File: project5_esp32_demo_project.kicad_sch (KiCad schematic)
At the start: 0 parts

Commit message: 1.1.2 Lipo battery charger
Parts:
- added J1: SS-52400-002, SS-52400-002:BELFUSE_SS-52400-002, symbol SS-52400-002:SS-52400-002
- added J2: B2B-PH-SM4-TB, B2B-PH-SM4-TB:JST_B2B-PH-SM4-TB, symbol B2B-PH-SM4-TB:B2B-PH-SM4-TB
- added LED1: LTST-C170KRKT, LTST-C170KRKT:DIOC200X125X110, symbol LTST-C170KRKT:LTST-C170KRKT
- added LED2: LTST-C170GKT, LED_LTST-C170GKT_LTO, symbol LTST-C170GKT:LTST-C170GKT
- added LED3: LTST-C170TBKT, LTST-C170TBKT:DIOC200X125X110, symbol LTST-C170TBKT:LTST-C170TBKT
- added R1, R2: 10K, symbol Device:R
- added R3, R4: 5K1, symbol Device:R
- added R5: 2K, symbol Device:R
- added R6: 20K, symbol Device:R
- added R7, R8, R9: 470, symbol Device:R
- added U1: MCP73871-2CAI_ML, MCP73871-2CAI_ML:QFN50P400X400X100-21N, symbol MCP73871-2CAI_ML:MCP73871-2CAI_ML
- added VR1: LM1117MPX-3.3, LM1117MPX-3.3:VREG_LM1117MPX-3.3, symbol LM1117MPX-3.3:LM1117MPX-3.3
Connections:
- new net: R6.2, U1.12 (PROG3)
- new net: J1.A5 (CC1), R4.1
- new net: J1.B5 (CC2), R3.1
- new net: LED2.1, R9.1
- new net: LED1.-, R7.1
- new net: R7.2, U1.7 (STAT2)
- new net: R1.1, U1.9 (~{TE})
- new net: R9.2, U1.6 (~{PG})
- new net: LED3.-, R8.1
- new net: U1.1 (OUT), U1.20 (OUT)
- new net: R5.1, U1.13 (PROG1)
- new net: U1.14 (VBAT), U1.15 (VBAT)
- new net: U1.18 (IN), U1.19 (IN)
- new net: R2.1, U1.5 (THERM)
- new net: R8.2, U1.8 (STAT1/~{LBO})
- new net GND: J1.A1 (GNDA1), J1.A12 (GNDA2), J1.B1 (GNDB1), J1.B12 (GNDB2), J1.G1 (GND/SHIELD), J1.G2 (GND/SHIELD), J1.G3 (GND/SHIELD), J1.G4 (GND/SHIELD), J1.S1 (GND/SHIELD), J1.S2 (GND/SHIELD), J1.S3 (GND/SHIELD), J1.S4 (GND/SHIELD), R1.2, R2.2, R3.2, R4.2, R5.2, R6.1
- new net VSS: U1.10 (VSS), U1.11 (VSS), U1.21 (VSS)

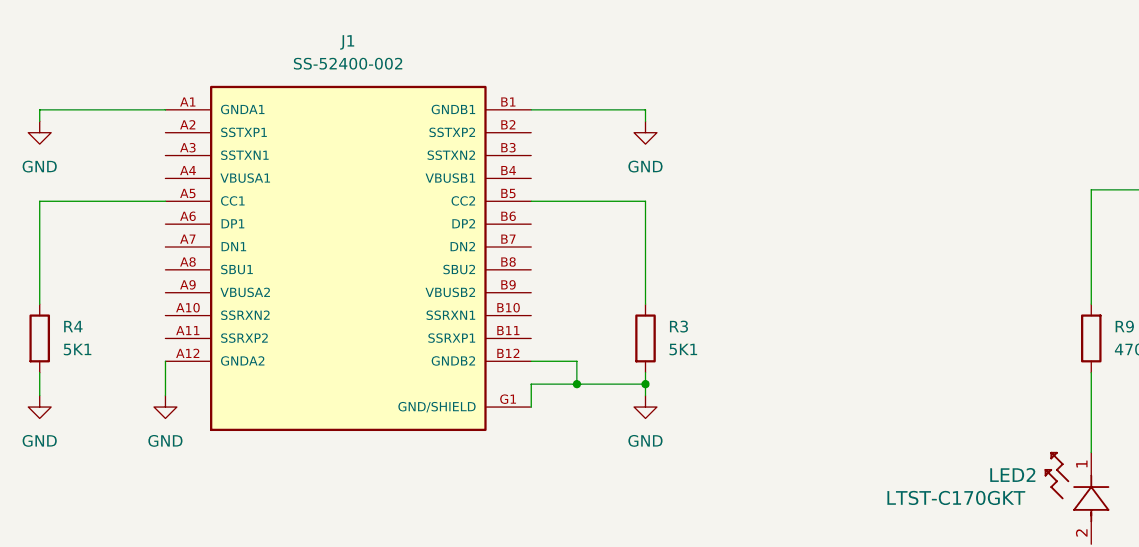
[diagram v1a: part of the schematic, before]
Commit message: 1.1.3 Design USB port subcircuit
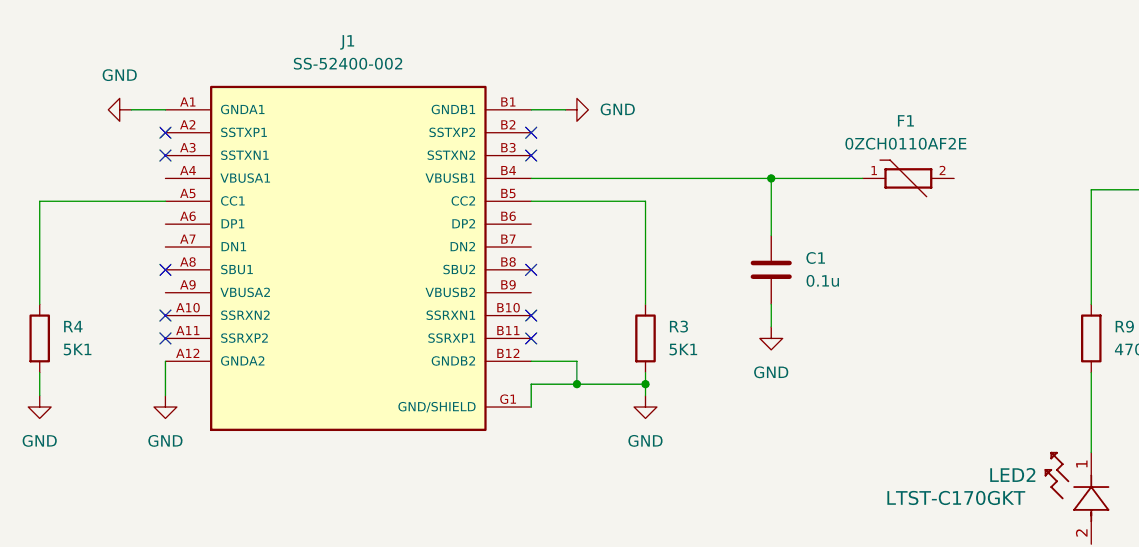
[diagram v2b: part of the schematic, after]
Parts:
- added C1: 0.1u, symbol Device:C
- added F1: 0ZCH0110AF2E, 0ZCH0110AF2E:FUSC3225X100N, symbol 0ZCH0110AF2E:0ZCH0110AF2E
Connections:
- net GND: now also C1.2
- net at J1.B4 (VBUSB1): now also C1.1, F1.1
- no-connect marks 0 -> 10

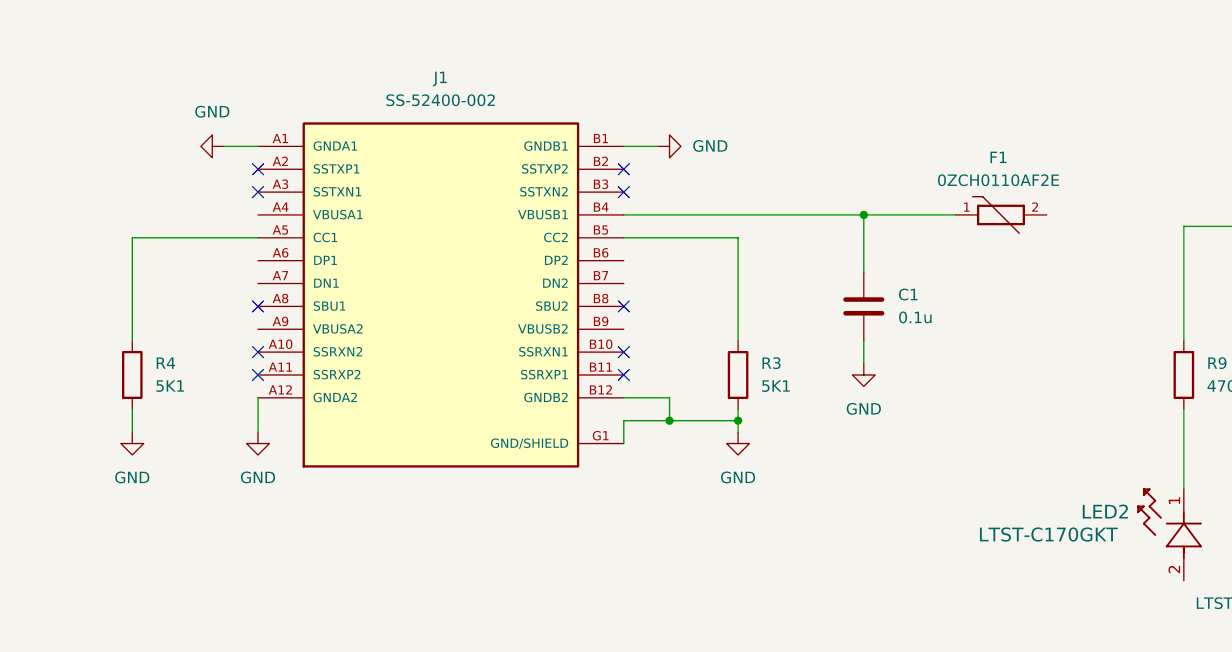
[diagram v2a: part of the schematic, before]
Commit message: 1.1.4 Create the first few nets
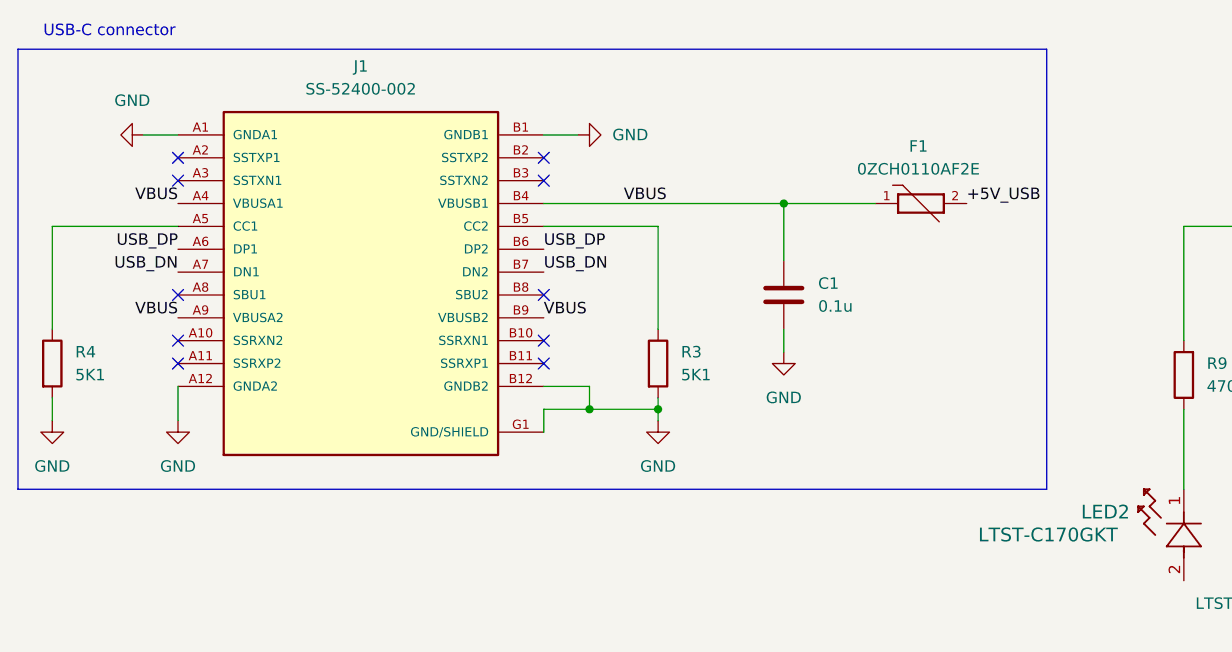
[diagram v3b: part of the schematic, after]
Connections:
- net VBUS: now reaches J1.A4 (VBUSA1)
- net VBUS: now also C1.1, F1.1, J1.A9 (VBUSA2), J1.B4 (VBUSB1), J1.B9 (VBUSB2)
- net USB_DP: now reaches J1.A6 (DP1)
- net USB_DP: now also J1.B6 (DP2)
- net USB_DN: now reaches J1.A7 (DN1)
- net USB_DN: now also J1.B7 (DN2)
- net +5V_USB: now reaches F1.2
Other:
- note added: "USB-C connector"
- moved on the sheet: C1, F1, J1, R3, R4

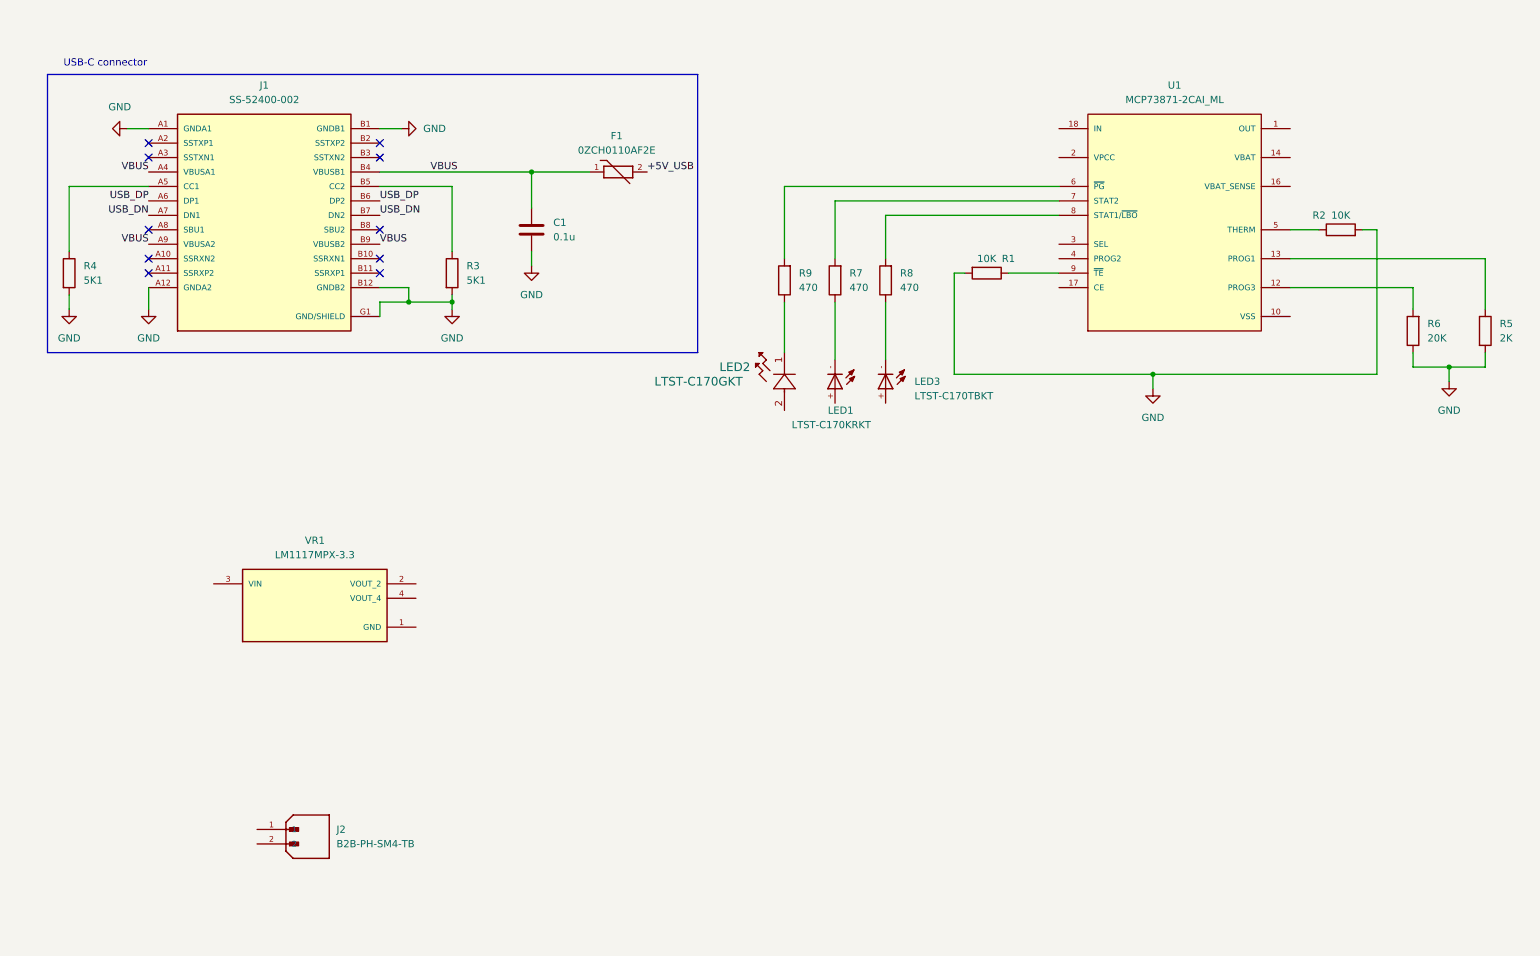
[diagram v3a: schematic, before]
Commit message: 1.1.5 Finish the design for the LiPo charger
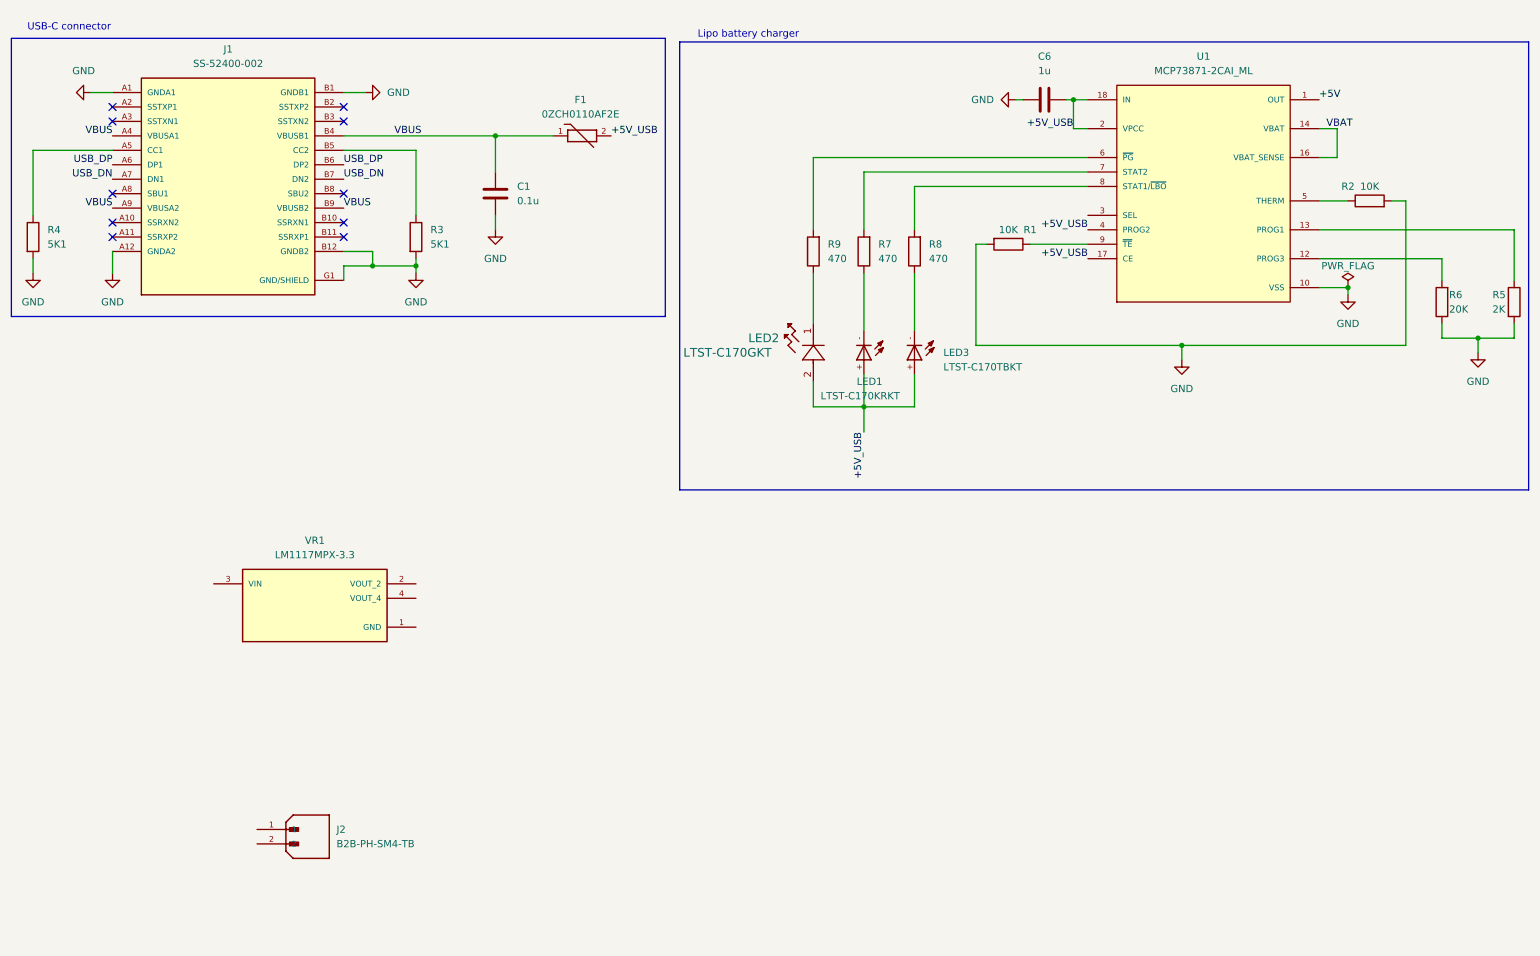
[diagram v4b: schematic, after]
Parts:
- added C6: 1u, symbol Device:C
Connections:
- net VSS is gone; now on net GND: U1.10 (VSS), U1.11 (VSS), U1.21 (VSS)
- net +5V_USB: now also LED1.+, LED2.2, LED3.+, U1.17 (CE), U1.18 (IN), U1.19 (IN), U1.2 (VPCC), U1.4 (PROG2), C6.2
- net GND: now also C6.1
- net +5V: now reaches U1.1 (OUT), U1.20 (OUT)
- net VBAT: now reaches U1.14 (VBAT), U1.15 (VBAT)
- net VBAT: now also U1.16 (VBAT_SENSE)
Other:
- note added: "Lipo battery charger"
- moved on the sheet: C1, F1, J1, LED1, LED2, LED3, R1, R2, R3, R4, R5, R6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

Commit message: 1.1.6 Design the voltage regulator subcircuit
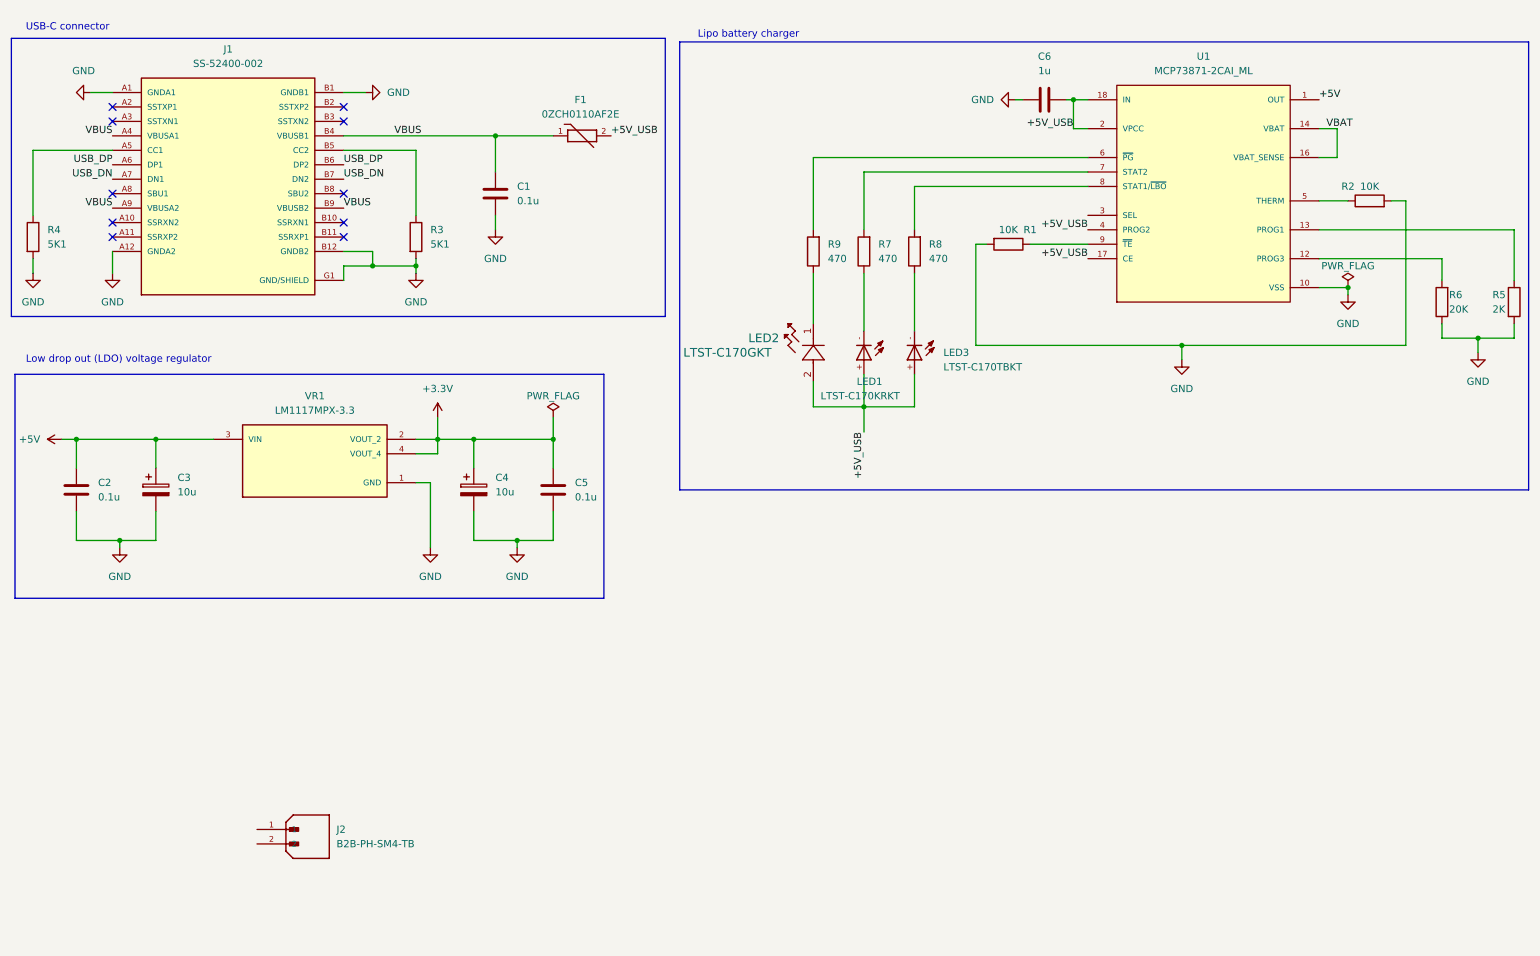
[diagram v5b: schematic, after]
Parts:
- added C2, C5: 0.1u, symbol Device:C
- added C3, C4: 10u, symbol Device:C_Polarized
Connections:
- net +5V: now also VR1.3 (VIN), C2.1, C3.1
- net GND: now also VR1.1 (GND), C2.2, C3.2, C4.2, C5.2
- net +3.3V: now reaches VR1.2 (VOUT_2)
- net +3.3V: now also VR1.4 (VOUT_4), C4.1, C5.1
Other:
- note added: "Low drop out (LDO) voltage regulator"
- moved on the sheet: VR1

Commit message: 1.1.7 Design the battery connector subcircuit
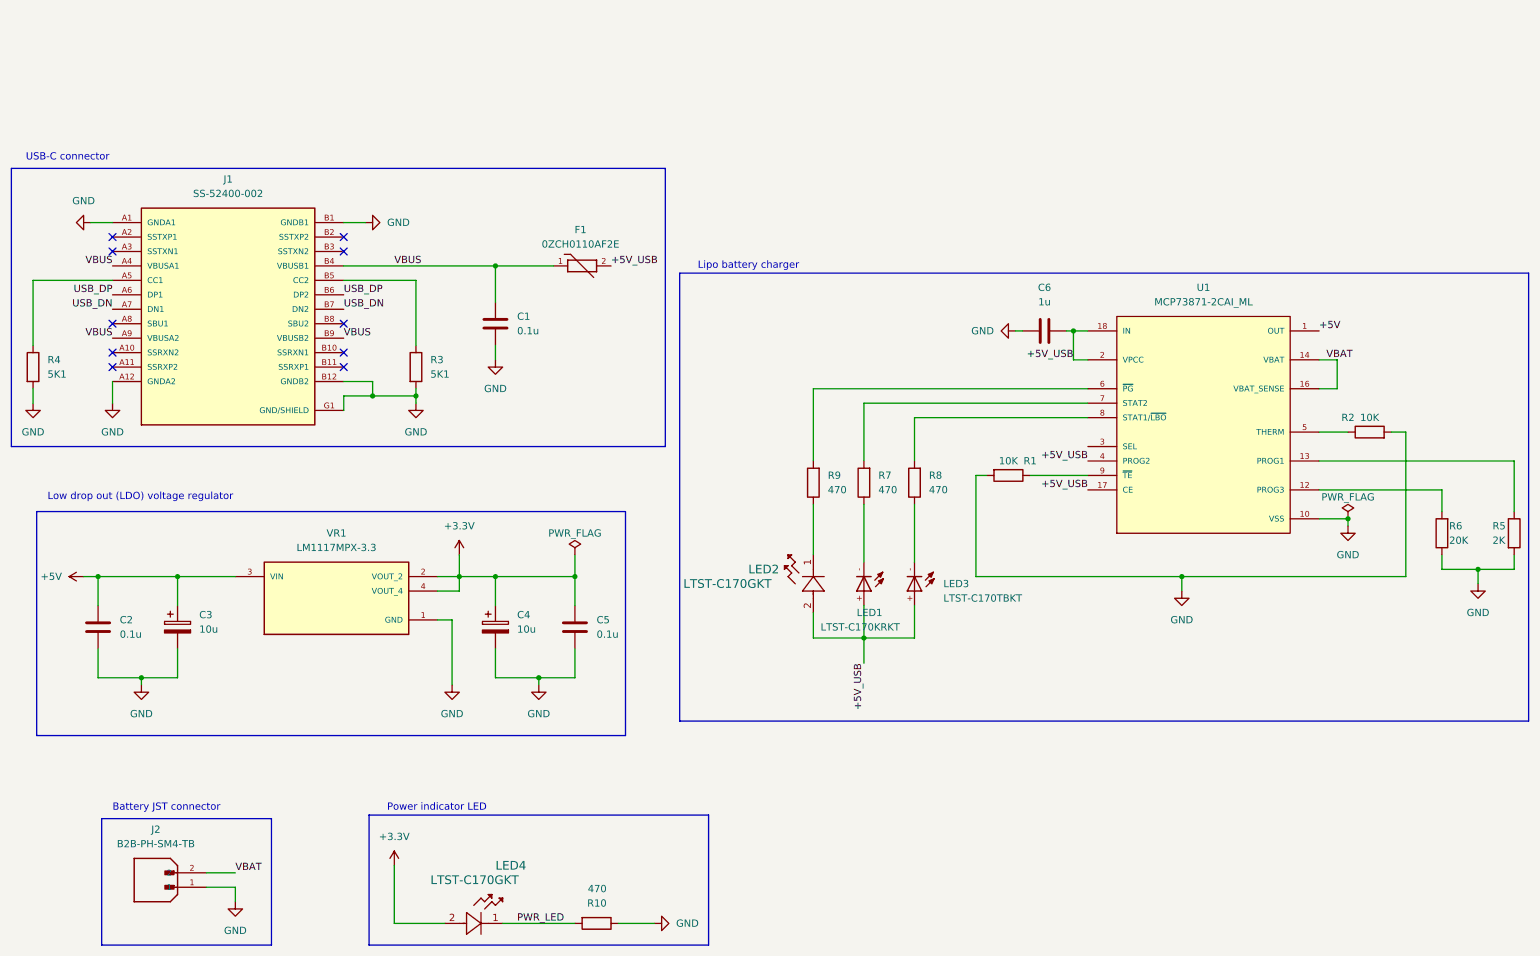
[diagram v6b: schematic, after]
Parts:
- added LED4: LTST-C170GKT, LED_LTST-C170GKT_LTO, symbol LTST-C170GKT:LTST-C170GKT
- added R10: 470, symbol Device:R
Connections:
- net +3.3V: now also LED4.2
- net GND: now also J2.1, R10.1
- net VBAT: now also J2.2
- new net PWR_LED: LED4.1, R10.2
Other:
- note added: "Battery JST connector"
- note added: "Power indicator LED"
- moved on the sheet: C1, C2, C3, C4, C5, C6, F1, J1, J2, LED1, LED2, LED3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
